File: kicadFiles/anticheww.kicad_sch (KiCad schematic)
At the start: 436 parts, among them J1 ARM JTAG, J2 TYPE-C-31-M-12, J3 Extra pins, Q1 AO3401A, Q2 DTC123JKAT146, Q3 DTC123JKAT146, SW1 ESC, SW10 9, SW11 0, SW12 MINUS, SW13 PLUS, SW14 LBKSP, SW15 RBKSP, SW16 2U_BKSP, SW17 TAB, SW18 Q, SW19 W, SW2 1, SW20 E, SW21 R, SW22 T, SW23 Y, SW24 U, SW25 I, SW26 O, SW27 P, SW28 LBRKT, SW29 RBRKT, SW3 2, SW30 BKSLSH, SW31 PGUP, SW32 ISO_ENTER, SW33 CAPS, SW34 A, SW35 S, SW36 D, SW37 F, SW38 G, SW39 H, SW4 3, SW40 J, SW41 K, SW42 L, SW43 COLON, SW44 QUOTE, SW45 ENTER, SW46 HOME, SW47 PGDN, SW48 STEPPED_CAPS, SW49 ISO_TILDE, SW5 4, SW50 LSHFT, SW51 ISO_BKLSH, SW52 Z, SW53 X, SW54 C, SW55 V, SW56 B, SW57 N, SW58 M, SW59 COMMA, SW6 5, SW60 DOT, SW61 SLSH, SW62 175_RSHFT, SW63 UP, SW64 END, SW65 ISO_LSHFT, SW66 275_RSHFT, SW67 LCTRL_125, SW68 LGUI_125, SW69 LALT_125, SW7 6, SW70 SPC_625, SW71 RALT_100, SW72 RGUI_100, SW73 RCTRL_100, SW74 LEFT, SW75 DOWN, SW76 RIGHT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

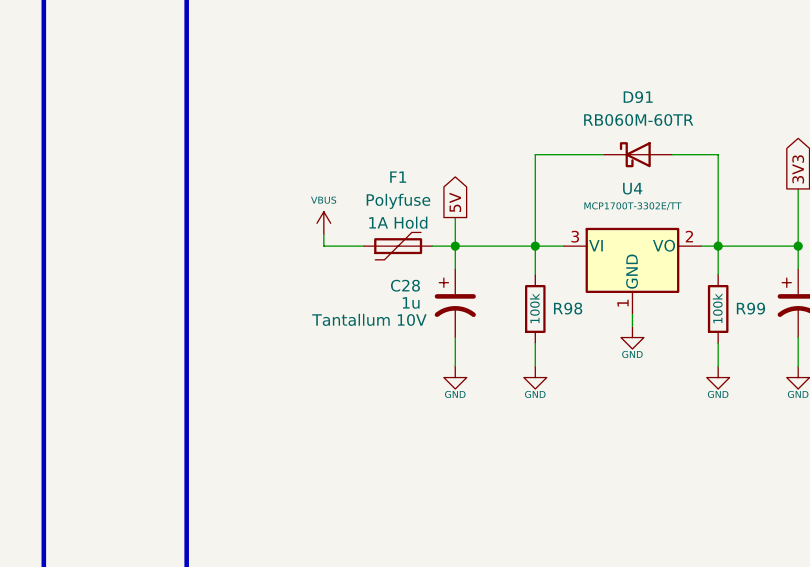
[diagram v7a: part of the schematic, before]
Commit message: Added missing fields for fuse F1. Preparing for release 2.0.8
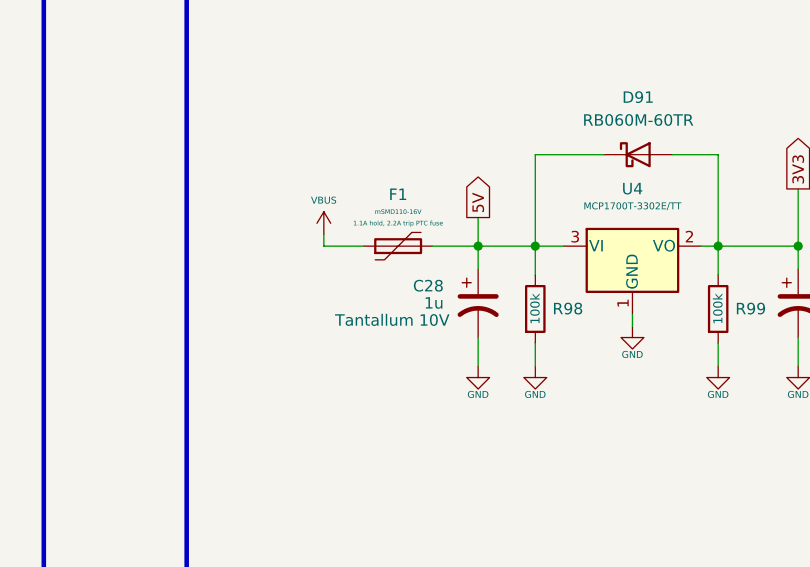
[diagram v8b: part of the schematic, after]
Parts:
- F1: value Polyfuse -> mSMD110-16V; LCSC Part Number (none) -> C69691; Manufacturer (none) -> TECHFUSE; Manufacturer Part Number (none) -> mSMD110-16V; Rating 1A Hold -> (none); Specification (none) -> 1.1A hold, 2.2A trip PTC fuse
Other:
- moved on the sheet: C28
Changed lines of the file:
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@@
   (title_block
     (title "Anticheww")
-    (date "2020-08-01")
-    (rev "V2.0.8.1")
+    (date "2020-08-02")
+    (rev "V2.0.8.3")
     (company "Designed by Gondolindrim")
     (comment 1 "In partnership with Chewwy")
@@
   (junction (at 406.4 146.05) (diameter 1.016) (color 0 0 0 0))
   (junction (at 406.4 177.8) (diameter 1.016) (color 0 0 0 0))
-  (junction (at 411.48 469.9) (diameter 1.016) (color 0 0 0 0))
+  (junction (at 414.02 469.9) (diameter 1.016) (color 0 0 0 0))
   (junction (at 419.1 69.85) (diameter 1.016) (color 0 0 0 0))
   (junction (at 419.1 101.6) (diameter 1.016) (color 0 0 0 0))
@@
     (stroke (width 0) (type solid) (color 0 0 0 0))
   )
-  (wire (pts (xy 408.94 469.9) (xy 411.48 469.9))
+  (wire (pts (xy 408.94 469.9) (xy 414.02 469.9))
     (stroke (width 0) (type solid) (color 0 0 0 0))
   )
-  (wire (pts (xy 411.48 466.725) (xy 411.48 469.9))
+  (wire (pts (xy 414.02 466.725) (xy 414.02 469.9))
     (stroke (width 0) (type solid) (color 0 0 0 0))
   )
-  (wire (pts (xy 411.48 469.9) (xy 411.48 472.44))
+  (wire (pts (xy 414.02 469.9) (xy 414.02 472.44))
     (stroke (width 0) (type solid) (color 0 0 0 0))
   )
-  (wire (pts (xy 411.48 469.9) (xy 420.37 469.9))
+  (wire (pts (xy 414.02 469.9) (xy 420.37 469.9))
     (stroke (width 0) (type solid) (color 0 0 0 0))
   )
-  (wire (pts (xy 411.48 480.06) (xy 411.48 483.235))
+  (wire (pts (xy 414.02 480.06) (xy 414.02 483.235))
     (stroke (width 0) (type solid) (color 0 0 0 0))
   )
@@
     (effects (font (size 1.016 1.016)) (justify left))
   )
-  (global_label "5V" (shape output) (at 411.48 466.725 90)
+  (global_label "5V" (shape output) (at 414.02 466.725 90)
     (effects (font (size 1.27 1.27)) (justify left))
   )
@@
     )
   )
-  (symbol (lib_id "power:GND") (at 411.48 483.235 0) (unit 1)
+  (symbol (lib_id "power:GND") (at 414.02 483.235 0) (unit 1)
     (in_bom yes) (on_board yes)
-    (property "Reference" "#PWR0141" (id 0) (at 411.48 489.585 0)
+    (property "Reference" "#PWR0141" (id 0) (at 414.02 489.585 0)
       (effects (font (size 1.27 1.27)) hide)
     )
-    (property "Value" "GND" (id 1) (at 411.48 486.41 0)
+    (property "Value" "GND" (id 1) (at 414.02 486.41 0)
       (effects (font (size 0.762 0.762)))
     )
-    (property "Footprint" "" (id 2) (at 411.48 483.235 0)
+    (property "Footprint" "" (id 2) (at 414.02 483.235 0)
       (effects (font (size 1.27 1.27)) hide)
     )
-    (property "Datasheet" "" (id 3) (at 411.48 483.235 0)
+    (property "Datasheet" "" (id 3) (at 414.02 483.235 0)
       (effects (font (size 1.27 1.27)) hide)
     )
@@
   (symbol (lib_id "Device:Polyfuse") (at 405.13 469.9 90) (unit 1)
     (in_bom yes) (on_board yes)
-    (property "Reference" "F1" (id 0) (at 405.13 462.28 90))
-    (property "Value" "Polyfuse" (id 1) (at 405.13 464.82 90))
+    (property "Reference" "F1" (id 0) (at 405.13 464.185 90))
+    (property "Value" "mSMD110-16V" (id 1) (at 405.13 466.09 90)
+      (effects (font (size 0.508 0.508)))
+    )
     (property "Footprint" "Fuse:Fuse_1812_4532Metric" (id 2) (at 410.21 468.63 0)
       (effects (font (size 1.27 1.27)) (justify left) hide)
@@
       (effects (font (size 1.27 1.27)) hide)
     )
-    (property "Rating" "1A Hold" (id 4) (at 405.13 467.36 90))
+    (property "Specification" "1.1A hold, 2.2A trip PTC fuse" (id 4) (at 405.13 467.36 90)
+      (effects (font (size 0.508 0.508)))
+    )
+    (property "Manufacturer" "TECHFUSE" (id 6) (at 405.13 469.9 90)
+      (effects (font (size 1.27 1.27)) hide)
+    )
+    (property "Manufacturer Part Number" "mSMD110-16V" (id 7) (at 405.13 469.9 90)
+      (effects (font (size 1.27 1.27)) hide)
+    )
+    (property "LCSC Part Number" "C69691" (id 8) (at 405.13 469.9 90)
+      (effects (font (size 1.27 1.27)) hide)
+    )
   )
   (symbol (lib_id "Switch:SW_SPST") (at 522.605 465.455 0) (unit 1)
@@
     )
   )
-  (symbol (lib_id "Device:CP1") (at 411.48 476.25 0) (unit 1)
+  (symbol (lib_id "Device:CP1") (at 414.02 476.25 0) (unit 1)
     (in_bom yes) (on_board yes)
-    (property "Reference" "C28" (id 0) (at 407.67 474.345 0)
+    (property "Reference" "C28" (id 0) (at 410.21 474.345 0)
       (effects (font (size 1.27 1.27)) (justify right))
     )
-    (property "Value" "1u" (id 1) (at 407.67 476.25 0)
+    (property "Value" "1u" (id 1) (at 410.21 476.25 0)
       (effects (font (size 1.27 1.27)) (justify right))
     )
-    (property "Footprint" "acheron_Components:CP_EIA-3216-10_Kemet-I_Pad1.58x1.35mm_HandSolder" (id 2) (at 411.48 476.25 0)
+    (property "Footprint" "acheron_Components:CP_EIA-3216-10_Kemet-I_Pad1.58x1.35mm_HandSolder" (id 2) (at 414.02 476.25 0)
       (effects (font (size 1.27 1.27)) hide)
     )
-    (property "Datasheet" "~" (id 3) (at 411.48 476.25 0)
+    (property "Datasheet" "~" (id 3) (at 414.02 476.25 0)
       (effects (font (size 1.27 1.27)) hide)
     )
-    (property "Package" "C3216" (id 4) (at 411.48 476.25 0)
+    (property "Package" "C3216" (id 4) (at 414.02 476.25 0)
       (effects (font (size 1.27 1.27)) hide)
     )
-    (property "Specification" "Tantallum 10V" (id 5) (at 408.305 478.155 0)
+    (property "Specification" "Tantallum 10V" (id 5) (at 410.845 478.155 0)
       (effects (font (size 1.27 1.27)) (justify right))
     )
